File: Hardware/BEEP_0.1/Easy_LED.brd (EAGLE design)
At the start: 46.9 x 33 mm, 12 parts, among them IC2 74HC238D

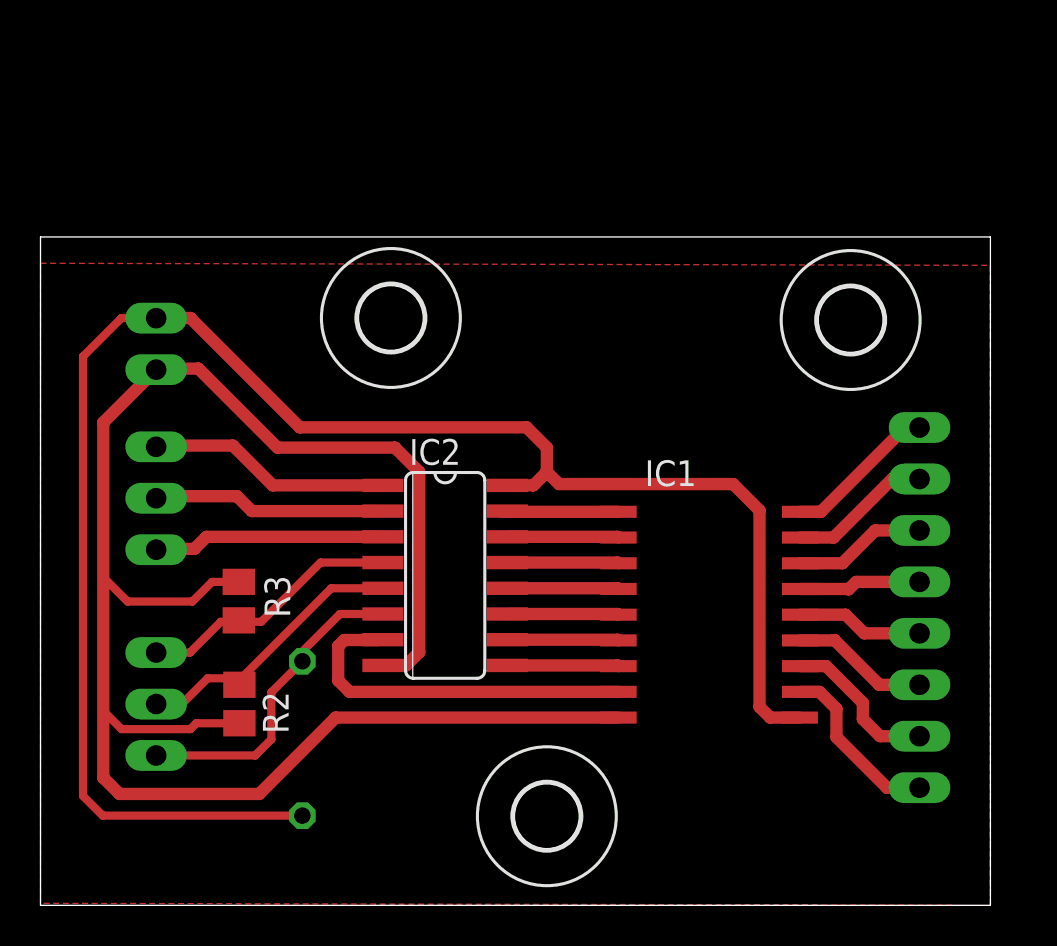
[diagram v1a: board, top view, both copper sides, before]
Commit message: Add branding ;) enhance PCBs finish Easy RGB Board add Texas Instruments libray from Element 14 add dxf import ulp for eagle add Script for easy eagle export to pdf for etching minor cleanup
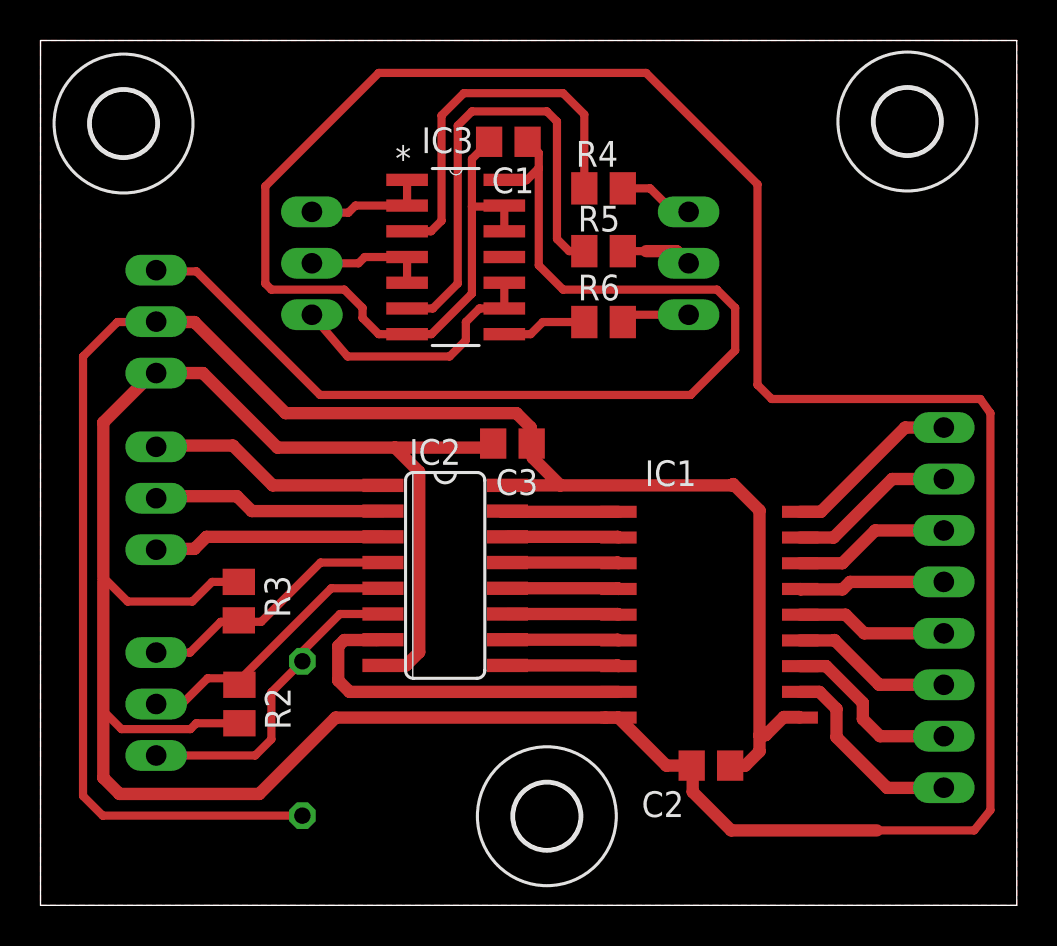
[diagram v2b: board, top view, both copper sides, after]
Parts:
- added C1, C2, C3: 100n, rcl:C0805
- added IC3: SN74ACT00D, Texas Instruments_By_element14_Batch_1:SOIC127P600X175-14N
- added PWM_IN, PWM_OUT: (no value), pinhead:1X03
- added R4, R5, R6: 68R, rcl:M0805
- added U$4: LOGO-COPPER6, Branding:COPPER6
- IC1: value (none) -> ULN2803ASOP18
- PWR: device pinhead:1X02 -> pinhead:1X03
- R1, R2, R3: value (none) -> 10k
- moved U$3 16.3 mm to (4.10, 38.6)
- moved U$2 10.2 mm to (42.8, 38.7)
- moved JP1 1.20 mm to (44.6, 14.7)
- moved PWR 1.10 mm to (5.71, 28.8)
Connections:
- new net N$12: IC3.1, IC3.2, PWM_IN.3
- new net N$13: IC3.4, IC3.5, PWM_IN.2
- new net N$14: IC3.10, IC3.9, PWM_IN.1
- new net N$18: PWM_OUT.3, R6.2
- new net N$19: PWM_OUT.2, R5.2
- new net N$20: PWM_OUT.1, R4.2
- new net N$21: IC3.3, R4.1
- new net N$25: IC3.6, R5.1
- new net N$26: IC3.8, R6.1
- new net VDD: C1.1, IC3.14, PWR.1
- net GND: now also C1.2, C2.2, C3.2, IC3.12, IC3.13, IC3.7, PWR.3; no longer PWR.2
- net VCC: now also C2.1, C3.1, PWR.2; no longer PWR.1
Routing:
- net GND: track 95.8 -> 221.0 mm
- net VDD: track 0.00 -> 53.0 mm
- net N$25: track 0.00 -> 23.6 mm
- net N$21: track 0.00 -> 18.7 mm
- net N$14: track 0.00 -> 13.2 mm
- net N$12: track 0.00 -> 6.13 mm
- net N$13: track 0.00 -> 6.10 mm
- net VCC: track 85.9 -> 90.4 mm
- net N$26: track 0.00 -> 4.20 mm
- net N$20: track 0.00 -> 3.95 mm
- net N$19: track 0.00 -> 3.50 mm
- net N$18: track 0.00 -> 3.40 mm
- net N$5: track 6.81 -> 8.01 mm
- net N$6: track 7.79 -> 8.99 mm
- net N$4: track 6.27 -> 7.47 mm
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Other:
- board size 46.9 x 33 mm -> 48.2 x 42.7 mm
- board text added: "0V"
- board text added: "3,3V"
- board text added: "5V"
- board text added: "Easy LED v0.2"
- board text removed: "GND"
- board text removed: "VCC"
